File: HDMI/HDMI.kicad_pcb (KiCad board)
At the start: 2 copper layers, 43 x 26 mm, 18 parts, among them J1 HDMI, J2 PMOD, U1 NCP1402SN33T1G

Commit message: Fixing pinouts and pictures
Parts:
- moved G*** 2.40 mm to (141.0, 76.2)
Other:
- board text added: "3v3"
- board text added: "CLK+"
- board text added: "CLK-"
- board text added: "D0+"
- board text added: "D0-"
- board text added: "D1+"
- board text added: "D1-"
- board text added: "D2+"
- board text added: "D2-"
- board text added: "GND"
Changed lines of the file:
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@@
   (general
     (thickness 1.6)
-    (drawings 4)
+    (drawings 18)
     (tracks 174)
     (zones 0)
@@
   (page A4)
   (layers
-    (0 F.Cu signal hide)
+    (0 F.Cu signal)
     (31 B.Cu signal hide)
     (32 B.Adhes user hide)
@@
   )
   (module parts:shutleworth (layer B.Cu)
-    (at 143.4 76.2 270)
+    (at 141 76.25 270)
     (fp_text reference G*** (at 0 0 270) (layer B.SilkS) hide
       (effects (font (size 1.524 1.524) (thickness 0.3)) (justify mirror))
@@
       (xy -9.506471 1.919111) (xy -9.508833 1.909074)) (layer B.SilkS) (width 0.01))
   )
+  (gr_text GND (at 147.5 74.25 180) (layer B.SilkS)
+    (effects (font (size 0.5 0.5) (thickness 0.1)) (justify mirror))
+  )
+  (gr_text CLK- (at 147.5 76.75 180) (layer B.SilkS)
+    (effects (font (size 0.5 0.5) (thickness 0.1)) (justify mirror))
+  )
+  (gr_text D2- (at 147.5 79.25 180) (layer B.SilkS)
+    (effects (font (size 0.5 0.5) (thickness 0.1)) (justify mirror))
+  )
+  (gr_text D1- (at 147.5 82 180) (layer B.SilkS)
+    (effects (font (size 0.5 0.5) (thickness 0.1)) (justify mirror))
+  )
+  (gr_text D0- (at 147.5 84.5 180) (layer B.SilkS)
+    (effects (font (size 0.5 0.5) (thickness 0.1)) (justify mirror))
+  )
+  (gr_text D0+ (at 150 84.5 180) (layer B.SilkS)
+    (effects (font (size 0.5 0.5) (thickness 0.1)) (justify mirror))
+  )
+  (gr_text D1+ (at 150 82 180) (layer B.SilkS)
+    (effects (font (size 0.5 0.5) (thickness 0.1)) (justify mirror))
+  )
+  (gr_text D2+ (at 150 79.25 180) (layer B.SilkS)
+    (effects (font (size 0.5 0.5) (thickness 0.1)) (justify mirror))
+  )
+  (gr_text CLK+ (at 150 76.75 180) (layer B.SilkS)
+    (effects (font (size 0.5 0.5) (thickness 0.1)) (justify mirror))
+  )
+  (gr_text GND (at 150 74.25 180) (layer B.SilkS)
+    (effects (font (size 0.5 0.5) (thickness 0.1)) (justify mirror))
+  )
+  (gr_text GND (at 150 71.75 180) (layer B.SilkS)
+    (effects (font (size 0.5 0.5) (thickness 0.1)) (justify mirror))
+  )
+  (gr_text GND (at 147.5 71.75 180) (layer B.SilkS)
+    (effects (font (size 0.5 0.5) (thickness 0.1)) (justify mirror))
+  )
+  (gr_text 3v3 (at 147.5 69.25 180) (layer B.SilkS)
+    (effects (font (size 0.5 0.5) (thickness 0.1)) (justify mirror))
+  )
+  (gr_text 3v3 (at 150 69.25 180) (layer B.SilkS)
+    (effects (font (size 0.5 0.5) (thickness 0.1)) (justify mirror))
+  )
   (gr_line (start 154 64) (end 154 90) (layer Edge.Cuts) (width 0.15))

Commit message: New versions
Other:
- outline, holes or cut-outs redrawn
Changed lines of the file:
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@@
   (general
     (thickness 1.6)
-    (drawings 16)
+    (drawings 20)
     (tracks 174)
     (zones 0)
@@
   (layers
     (0 F.Cu signal)
-    (31 B.Cu signal hide)
+    (31 B.Cu signal)
     (32 B.Adhes user hide)
     (33 F.Adhes user hide)
@@
     (visible_elements FFFFFF7F)
     (pcbplotparams
-      (layerselection 0x010fc_ffffffff)
+      (layerselection 0x010f0_ffffffff)
       (usegerberextensions false)
       (usegerberattributes false)
@@
       (outputformat 1)
       (mirror false)
-      (drillshape 1)
+      (drillshape 0)
       (scaleselection 1)
-      (outputdirectory ""))
+      (outputdirectory "Gerber/"))
   )
   (net 0 "")
@@
       (xy -9.506471 1.919111) (xy -9.508833 1.909074)) (layer B.SilkS) (width 0.01))
   )
+  (gr_line (start 122.25 90) (end 111 90) (layer Edge.Cuts) (width 0.15))
+  (gr_line (start 154 90) (end 125.75 90) (layer Edge.Cuts) (width 0.15))
+  (gr_line (start 125.75 64) (end 154 64) (layer Edge.Cuts) (width 0.15))
+  (gr_line (start 111 64) (end 122.25 64) (layer Edge.Cuts) (width 0.15))
+  (gr_arc (start 124 90) (end 125.75 90) (angle -180) (layer Edge.Cuts) (width 0.15))
+  (gr_arc (start 124 64) (end 122.25 64) (angle -180) (layer Edge.Cuts) (width 0.15))
   (gr_text GND (at 147.5 74.25 180) (layer B.SilkS)
     (effects (font (size 0.5 0.5) (thickness 0.1)) (justify mirror))
@@
   )
   (gr_line (start 154 64) (end 154 90) (layer Edge.Cuts) (width 0.15))
-  (gr_line (start 111 90) (end 154 90) (layer Edge.Cuts) (width 0.15))
   (gr_line (start 111 64) (end 111 90) (layer Edge.Cuts) (width 0.15))
-  (gr_line (start 154 64) (end 111 64) (layer Edge.Cuts) (width 0.15))
   (segment (start 135.261949 87.80625) (end 137.017678 86.050521) (width 0.2) (layer F.Cu) (net 1))
   (segment (start 132.5875 88.5) (end 133.28125 87.80625) (width 0.2) (layer F.Cu) (net 1))
@@
     (polygon
       (pts
-        (xy 154 90) (xy 111 90) (xy 111 64) (xy 154 64)
+        (xy 111 64) (xy 154 64) (xy 154 90) (xy 111 90)
       )
     )

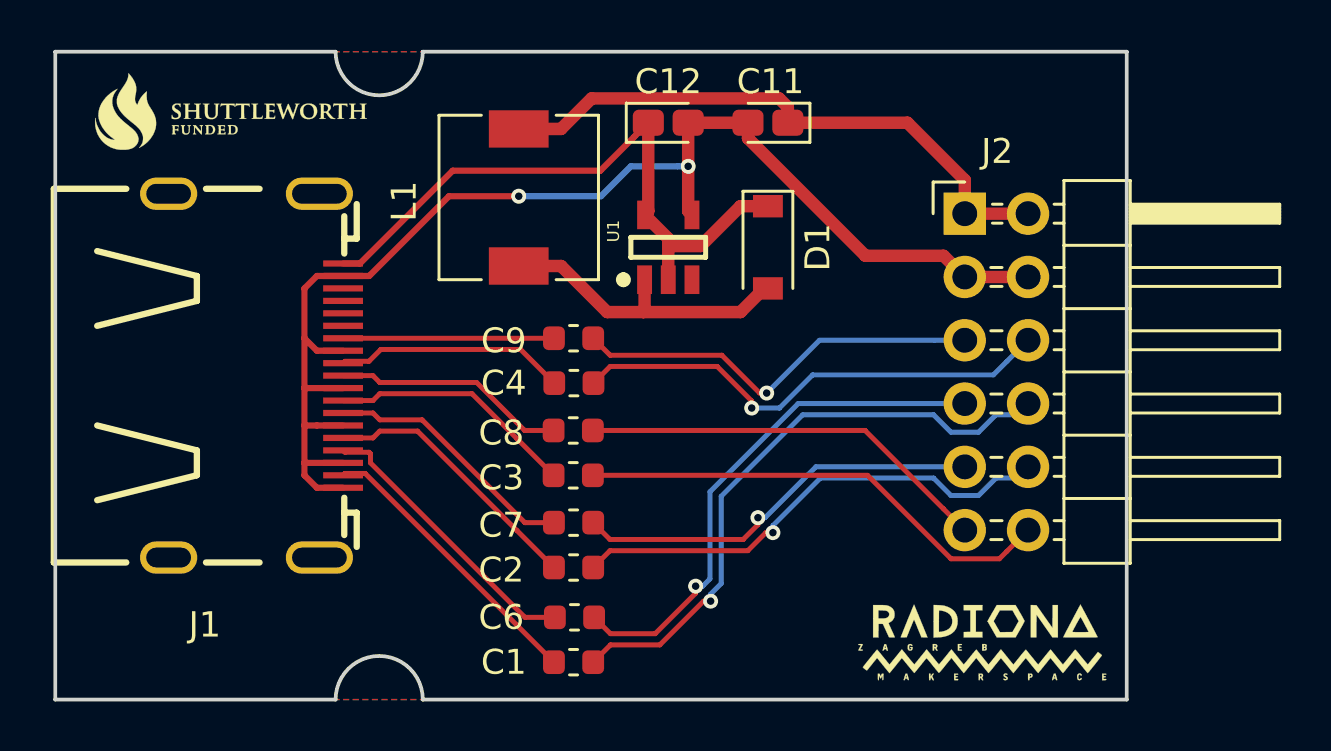
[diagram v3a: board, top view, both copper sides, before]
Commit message: Changing HDMI connector -- initial placement
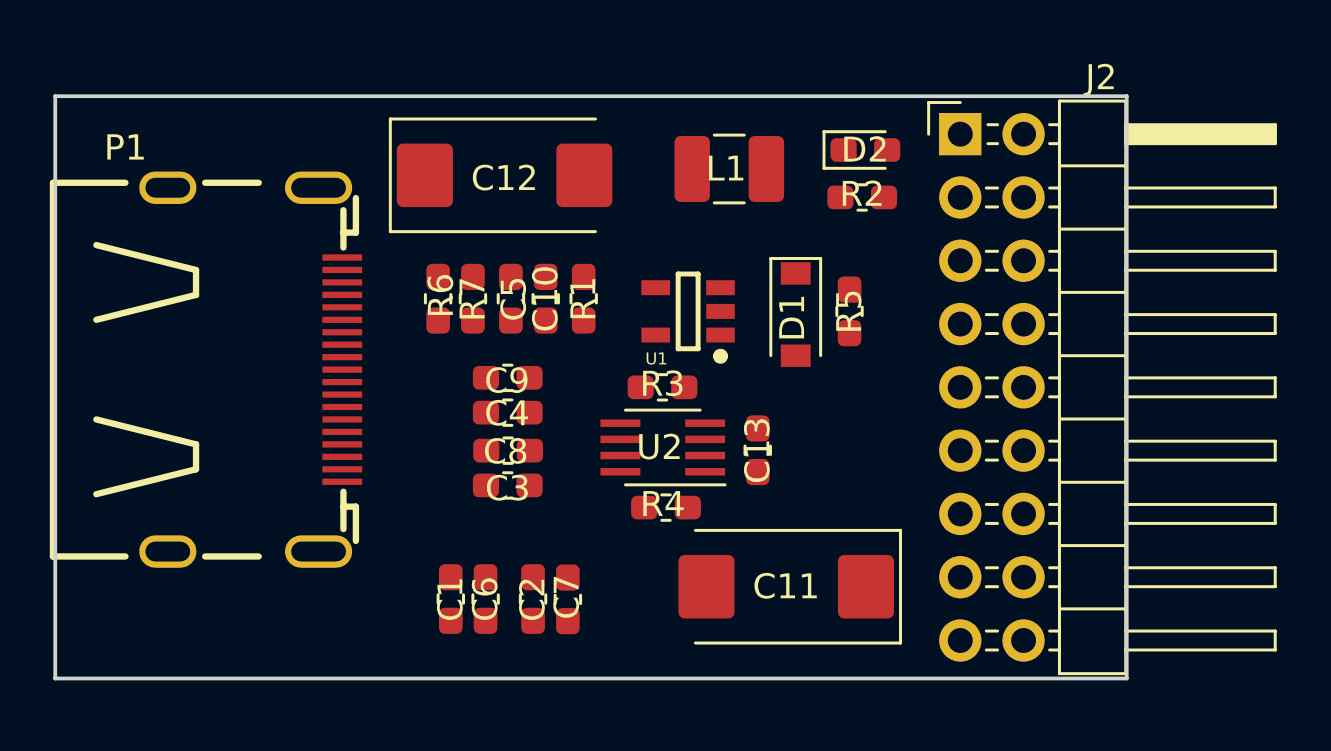
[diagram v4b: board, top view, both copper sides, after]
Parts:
- removed G***: LOGO, parts:radiona-12mm
- removed G***: LOGO, parts:shutleworth-12mm
- removed G***: LOGO, parts:shutleworth
- removed J1: HDMI, hdmi-swm-19:hdmi-swm-19
- added C10: 220nF, Capacitor_SMD:C_0603_1608Metric_Pad1.05x0.95mm_HandSolder, F.Cu at (130.7, 73.9)
- added C13: 470pF, Capacitor_SMD:C_0603_1608Metric_Pad1.05x0.95mm_HandSolder, F.Cu at (139.2, 80.0)
- added C5: 220nF, Capacitor_SMD:C_0603_1608Metric_Pad1.05x0.95mm_HandSolder, F.Cu at (129.3, 73.9)
- added D2: LED, LED_SMD:LED_0603_1608Metric_Pad1.05x0.95mm_HandSolder, F.Cu at (143.5, 67.9)
- added P1: HDMI-D, HDMI:HDMI-D, F.Cu at (117.0, 76.8)
- added R1: 510, Resistor_SMD:R_0603_1608Metric_Pad1.05x0.95mm_HandSolder, F.Cu at (132.2, 73.9)
- added R2: 4.7k, Resistor_SMD:R_0603_1608Metric_Pad1.05x0.95mm_HandSolder, F.Cu at (143.4, 69.8)
- added R3: 3.3k, Resistor_SMD:R_0603_1608Metric_Pad1.05x0.95mm_HandSolder, F.Cu at (135.4, 77.5)
- added R4: 3.3k, Resistor_SMD:R_0603_1608Metric_Pad1.05x0.95mm_HandSolder, F.Cu at (135.5, 82.3)
- added R5: 100k, Resistor_SMD:R_0603_1608Metric_Pad1.05x0.95mm_HandSolder, F.Cu at (142.9, 74.4)
- added R6: 4.7k, Resistor_SMD:R_0603_1608Metric_Pad1.05x0.95mm_HandSolder, F.Cu at (126.4, 73.9)
- added R7: 4.7k, Resistor_SMD:R_0603_1608Metric_Pad1.05x0.95mm_HandSolder, F.Cu at (127.8, 73.9)
- added U2: PCA9306, Package_SO:SSOP-8_2.95x2.8mm_P0.65mm, F.Cu at (135.4, 79.9)
- C1, C2, C3, C4, C6, C7, C8, C9: footprint Capacitor_SMD:C_0603_1608Metric -> Capacitor_SMD:C_0603_1608Metric_Pad1.05x0.95mm_HandSolder
- C11, C12: footprint Capacitor_Tantalum_SMD:CP_EIA-1608-08_AVX-J_Pad1.25x1.05mm_HandSolder -> Capacitor_Tantalum_SMD:CP_EIA-7343-15_Kemet-W_Pad2.25x2.55mm_HandSolder
- J2: footprint Connector_PinHeader_2.54mm:PinHeader_2x06_P2.54mm_Horizontal -> Connector_PinHeader_2.54mm:PinHeader_2x09_P2.54mm_Horizontal
- L1: footprint Inductor_SMD:L_6.3x6.3_H3 -> Inductor_SMD:L_1210_3225Metric_Pad1.42x2.65mm_HandSolder
- moved C11 18.6 mm to (140.3, 85.5)
- moved L1 8.53 mm to (138.0, 68.7), turned to 180 degrees
- moved C12 6.90 mm to (129.0, 69.0)
- moved C1 5.54 mm to (126.9, 86.0), turned to 90 degrees
- moved C6 3.64 mm to (128.3, 86.0), turned to 90 degrees
- moved J2 3.20 mm to (147.3, 67.3)
- moved C7 3.09 mm to (131.6, 86.0), turned to 90 degrees
- moved C9 3.08 mm to (129.2, 77.1)
- moved D1 2.92 mm to (140.7, 74.5)
- moved C4 2.91 mm to (129.2, 78.5)
- moved C8 2.74 mm to (129.2, 80.0)
- moved U1 2.69 mm to (136.4, 74.4), turned to 180 degrees
- moved C3 2.66 mm to (129.2, 81.4)
- moved C2 2.06 mm to (130.2, 86.0), turned to 90 degrees
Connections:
- C1 pad 1: FPDI_D2+ -> GPDI_D2+
- C1 pad 2: /GPDI_D2+ -> Net-(C1-Pad2)
- C2 pad 1: FPDI_D1+ -> GPDI_D1+
- C2 pad 2: /GPDI_D1+ -> Net-(C2-Pad2)
- C3 pad 1: FPDI_D0+ -> GPDI_D0+
- C3 pad 2: /GPDI_D0+ -> Net-(C3-Pad2)
- C4 pad 1: FPDI_CLK+ -> GPDI_CLK+
- C4 pad 2: /GPDI_CLK+ -> Net-(C4-Pad2)
- C6 pad 1: FPDI_D2- -> GPDI_D2-
- C6 pad 2: /GPDI_D2- -> Net-(C6-Pad2)
- C7 pad 1: FPDI_D1- -> GPDI_D1-
- C7 pad 2: /GPDI_D1- -> Net-(C7-Pad2)
- C8 pad 1: FPDI_D0- -> GPDI_D0-
- C8 pad 2: /GPDI_D0- -> Net-(C8-Pad2)
- C9 pad 1: FPDI_CLK- -> GPDI_CLK-
- C9 pad 2: /GPDI_CLK- -> Net-(C9-Pad2)
- J2 pad 1: +3V3 -> LED_HDMI
- J2 pad 10: FPDI_D1+ -> GPDI_D2+
- J2 pad 11: FPDI_D0- -> GPDI_CLK-
- J2 pad 12: FPDI_D0+ -> GPDI_CLK+
- J2 pad 2: +3V3 -> GPDI_CEC
- J2 pad 3: GND -> PMOD_SCL
- J2 pad 4: GND -> PMOD_SDA
- J2 pad 5: FPDI_CLK- -> GPDI_D0-
- J2 pad 6: FPDI_CLK+ -> GPDI_D0+
- J2 pad 7: FPDI_D2- -> GPDI_D1-
- J2 pad 8: FPDI_D2+ -> GPDI_D1+
- J2 pad 9: FPDI_D1- -> GPDI_D2-
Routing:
- net GND: track 53.4 -> 0.00 mm, vias 2 -> 0
- net +5V: track 26.0 -> 0.00 mm
- net FPDI_D2+: track 24.5 -> 0.00 mm, vias 1 -> 0
- net +3V3: track 24.0 -> 0.00 mm
- net FPDI_D2-: track 21.2 -> 0.00 mm, vias 1 -> 0
- net FPDI_D1+: track 19.9 -> 0.00 mm, vias 1 -> 0
- net FPDI_CLK+: track 19.7 -> 0.00 mm, vias 1 -> 0
- net FPDI_D0+: track 19.3 -> 0.00 mm
- net FPDI_CLK-: track 16.7 -> 0.00 mm, vias 1 -> 0
- net FPDI_D0-: track 16.6 -> 0.00 mm
- net FPDI_D1-: track 16.6 -> 0.00 mm, vias 1 -> 0
- net Net-(D1-Pad2): track 12.5 -> 0.00 mm
- net /GPDI_D2+: track 11.6 -> 0.00 mm
- net /GPDI_D2-: track 11.5 -> 0.00 mm
- net /GPDI_D1+: track 10.8 -> 0.00 mm
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- removed copper zone on B.Cu, net GND
- removed copper zone on F.Cu, net GND
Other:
- board size 43 x 26 mm -> 43 x 23.4 mm
- board text added: "3V3"
- board text added: "CEC"
- board text added: "ETH+"
- board text added: "ETH-"
- board text added: "LED"
- board text added: "SCL"
- board text added: "SDA"
- board text removed: "3v3"

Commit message: Finished routing HDMI INPUt
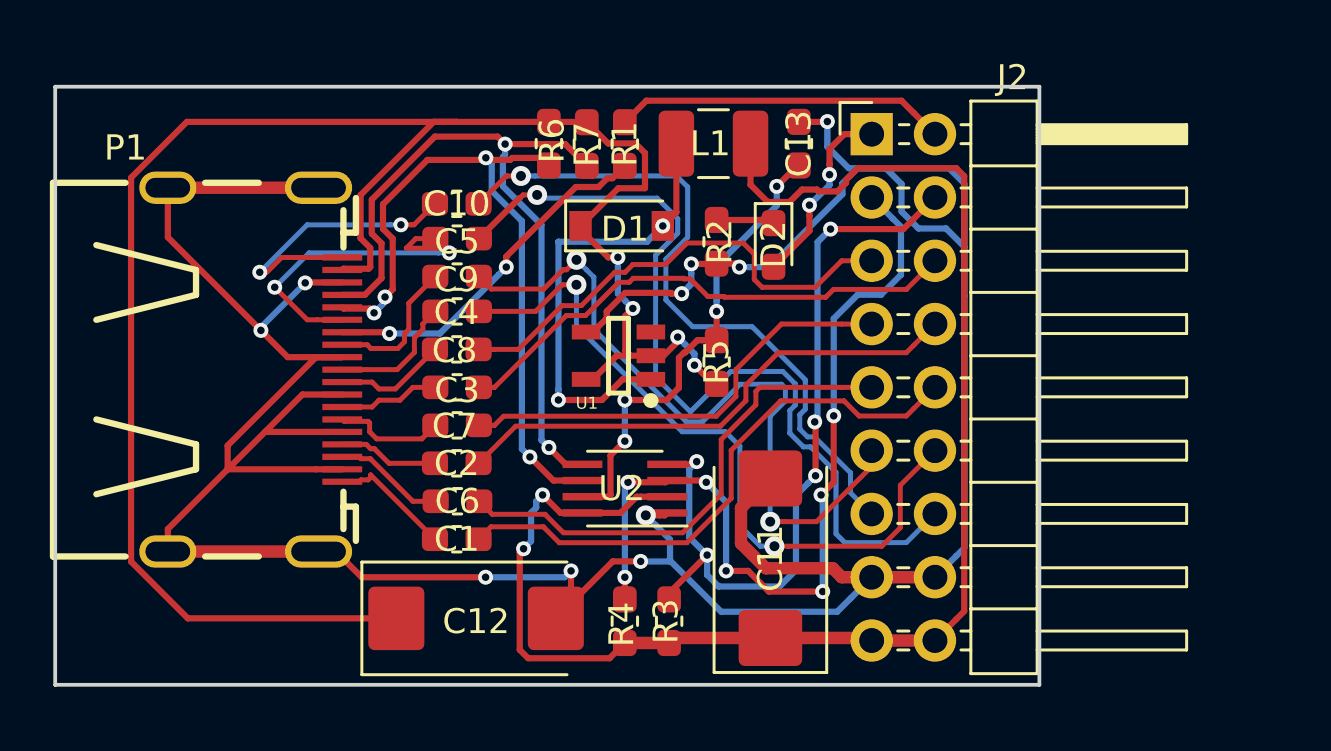
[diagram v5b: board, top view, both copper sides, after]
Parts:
- moved C12 17.8 mm to (127.9, 86.7)
- moved C13 12.4 mm to (140.8, 67.7), turned to 90 degrees
- moved R3 9.39 mm to (135.6, 86.9), turned to 90 degrees
- moved C7 8.28 mm to (127.1, 79.0), turned to 180 degrees
- moved D1 7.84 mm to (133.7, 71.0), turned to 0 degrees
- moved R7 7.71 mm to (132.3, 67.7)
- moved R6 7.65 mm to (130.8, 67.7)
- moved R1 6.42 mm to (133.9, 67.7)
- moved C2 6.25 mm to (127.1, 80.5), turned to 180 degrees
- moved R2 6.11 mm to (137.5, 71.6), turned to 270 degrees
- moved R5 5.71 mm to (137.5, 76.5), turned to 90 degrees
- moved D2 5.30 mm to (139.8, 71.8), turned to 270 degrees
- moved C10 5.22 mm to (127.1, 70.1), turned to 180 degrees
- moved R4 4.85 mm to (133.9, 86.9), turned to 90 degrees
- moved C8 4.56 mm to (127.1, 75.9)
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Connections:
- net Net-(C1-Pad2) renamed /D2+
- net Net-(C10-Pad2) renamed /ETH-
- net Net-(C2-Pad2) renamed /D1+
- net Net-(C3-Pad2) renamed /D0+
- net Net-(C4-Pad2) renamed /CLK+
- net Net-(C5-Pad2) renamed /ETH+
- net Net-(C6-Pad2) renamed /D2-
- net Net-(C7-Pad2) renamed /D1-
- net Net-(C8-Pad2) renamed /D0-
- net Net-(C9-Pad2) renamed /CLK-
- net Net-(P1-Pad13) renamed /CEC
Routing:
- net GND: track 0.00 -> 143.3 mm, vias 0 -> 10
- net +5V: track 0.00 -> 76.6 mm, vias 0 -> 4
- net +3V3: track 0.00 -> 59.8 mm, vias 0 -> 2
- net GPDI_ETH+: track 0.00 -> 34.5 mm, vias 0 -> 1
- net PMOD_SCL: track 0.00 -> 34.3 mm, vias 0 -> 7
- net PMOD_SDA: track 0.00 -> 31.6 mm, vias 0 -> 5
- net GPDI_SDA: track 0.00 -> 29.9 mm, vias 0 -> 2
- net GPDI_SCL: track 0.00 -> 29.0 mm, vias 0 -> 4
- net GPDI_CLK+: track 0.00 -> 28.5 mm, vias 0 -> 2
- net GPDI_CLK-: track 0.45 -> 28.8 mm, vias 0 -> 2
- net GPDI_ETH-: track 1.20 -> 27.7 mm, vias 0 -> 1
- net GPDI_D2+: track 0.00 -> 23.0 mm
- net GPDI_D0+: track 0.00 -> 21.0 mm
- net GPDI_D1+: track 0.00 -> 21.0 mm
- net GPDI_D2-: track 0.00 -> 20.3 mm
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- added copper zone on B.Cu, net GND
- added copper zone on F.Cu, net GND
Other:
- board size 43 x 23.4 mm -> 39.5 x 24 mm

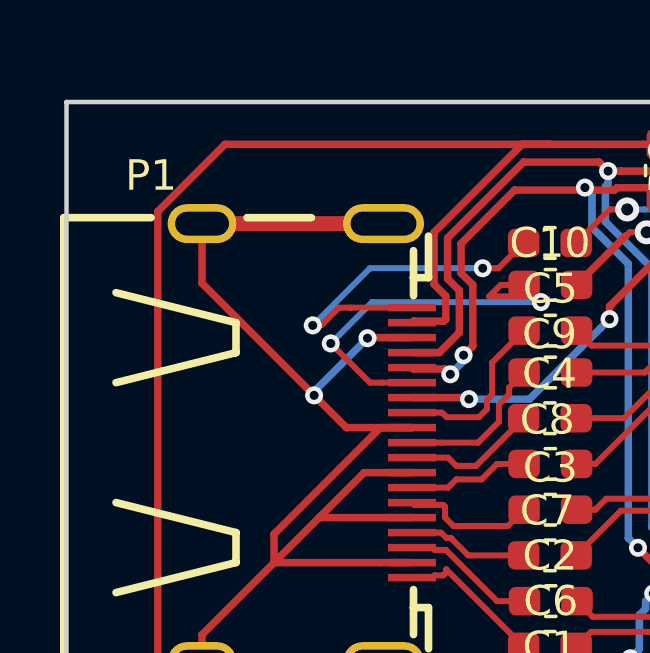
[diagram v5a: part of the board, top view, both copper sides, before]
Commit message: Adding logos
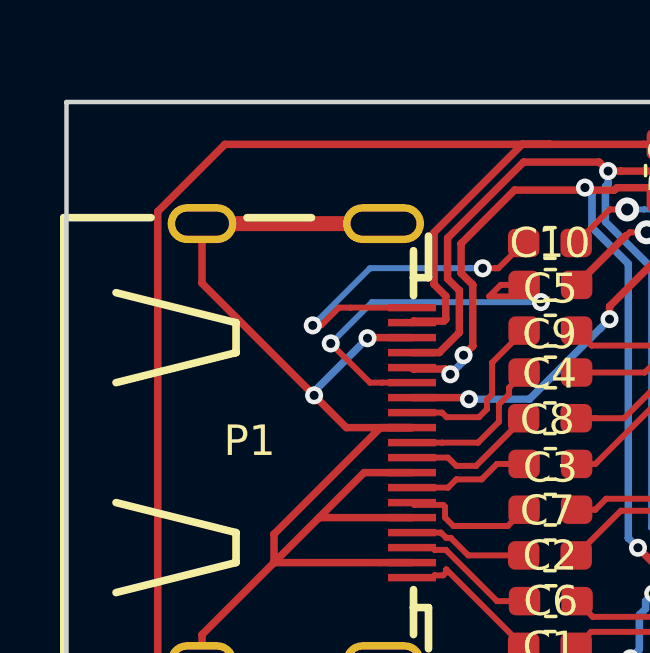
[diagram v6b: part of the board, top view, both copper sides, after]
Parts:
- added G***: LOGO, parts:shutleworth, B.Cu at (127.9, 69.2)
- added G***: LOGO, parts:radiona-16mm, B.Cu at (132.1, 86.1)

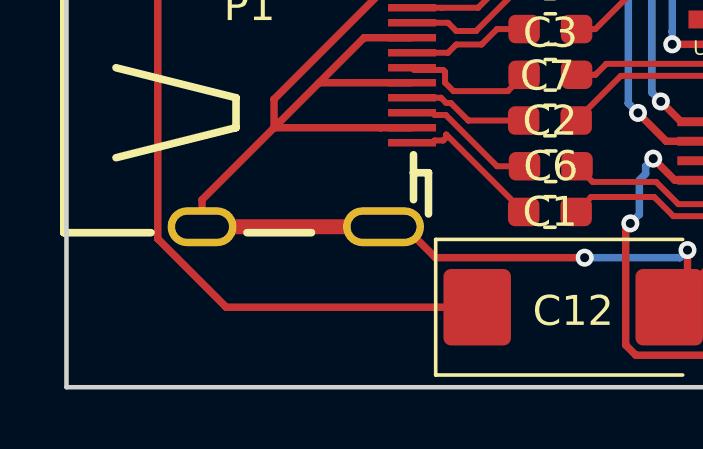
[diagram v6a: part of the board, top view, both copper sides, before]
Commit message: HDMI update
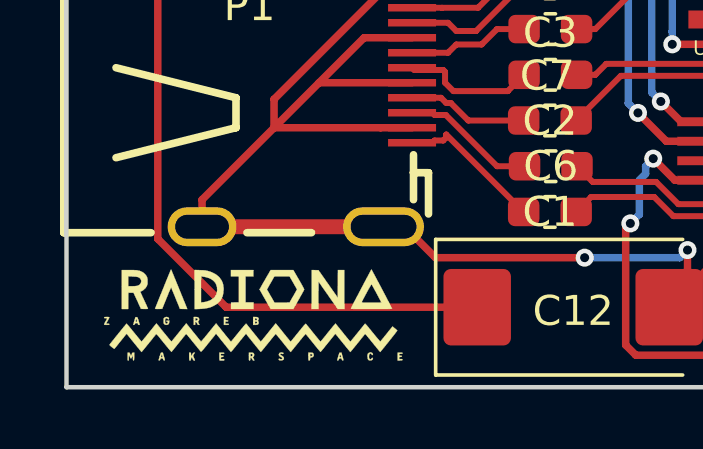
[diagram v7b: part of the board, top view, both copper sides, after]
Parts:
- added G***: LOGO, parts:radiona-10mm, F.Cu at (117.2, 87.0)

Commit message: Adding screws - adding OSH Park logos
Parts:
- removed the G*** at (117.2, 87.0)
- removed the G*** at (127.9, 69.2)
- removed the G*** at (132.1, 86.1)
- added G***: LOGO, parts2:OSH_10x10, B.Cu at (132.8, 83.1)
- added G***: LOGO, parts2:shutleworth, B.Cu at (127.3, 77.0)
- added G***: LOGO, parts2:radiona-16mm, B.Cu at (132.6, 69.1)
- added G***: LOGO, parts2:OSH_5x5, F.Cu at (114.8, 87.1)
- added G***: LOGO, parts2:shutleworth-12mm, F.Cu at (140.2, 83.6)
- added G***: LOGO, parts2:radiona-10mm, F.Cu at (118.9, 66.5)
- C11, C12: footprint Capacitor_Tantalum_SMD:CP_EIA-7343-15_Kemet-W_Pad2.25x2.55mm_HandSolder -> Capacitor_Tantalum_SMD:CP_EIA-3216-10_Kemet-I
- moved C11 14.1 mm to (125.8, 86.7), turned to 180 degrees
- moved C12 7.56 mm to (120.3, 86.7)
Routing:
- net GND: track 143.3 -> 135.3 mm
- net +5V: track 76.6 -> 70.9 mm
- net +3V3: track 59.8 -> 62.3 mm
- net /D1+: track 4.04 -> 5.23 mm
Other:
- board size 39.5 x 24 mm -> 39.5 x 25.1 mm
